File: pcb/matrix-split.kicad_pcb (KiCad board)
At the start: 2 copper layers, 160.1 x 127.5 mm, 115 parts, among them J1 AudioJack4, J4 DBG, SW1 Switch, SW10 Switch, SW11 Switch, SW12 Switch, SW13 Switch, SW14 Switch, SW15 Switch, SW16 Switch, SW17 Switch, SW18 Switch, SW19 Switch, SW2 Switch, SW20 Switch, SW21 Switch, SW22 Switch, SW23 Switch, SW24 Switch, SW25 Switch, SW26 Switch, SW27 Switch, SW28 Switch, SW29 Switch, SW3 Switch, SW30 Reset_Switch, SW31 BootSel_Switch, SW4 Switch, SW5 Switch, SW6 Switch, SW7 Switch, SW8 Switch, SW9 Switch, U1 W25Q128JVS, U2 RP2040, U3 NCP1117-3.3_SOT223, Y1 Crystal_GND24

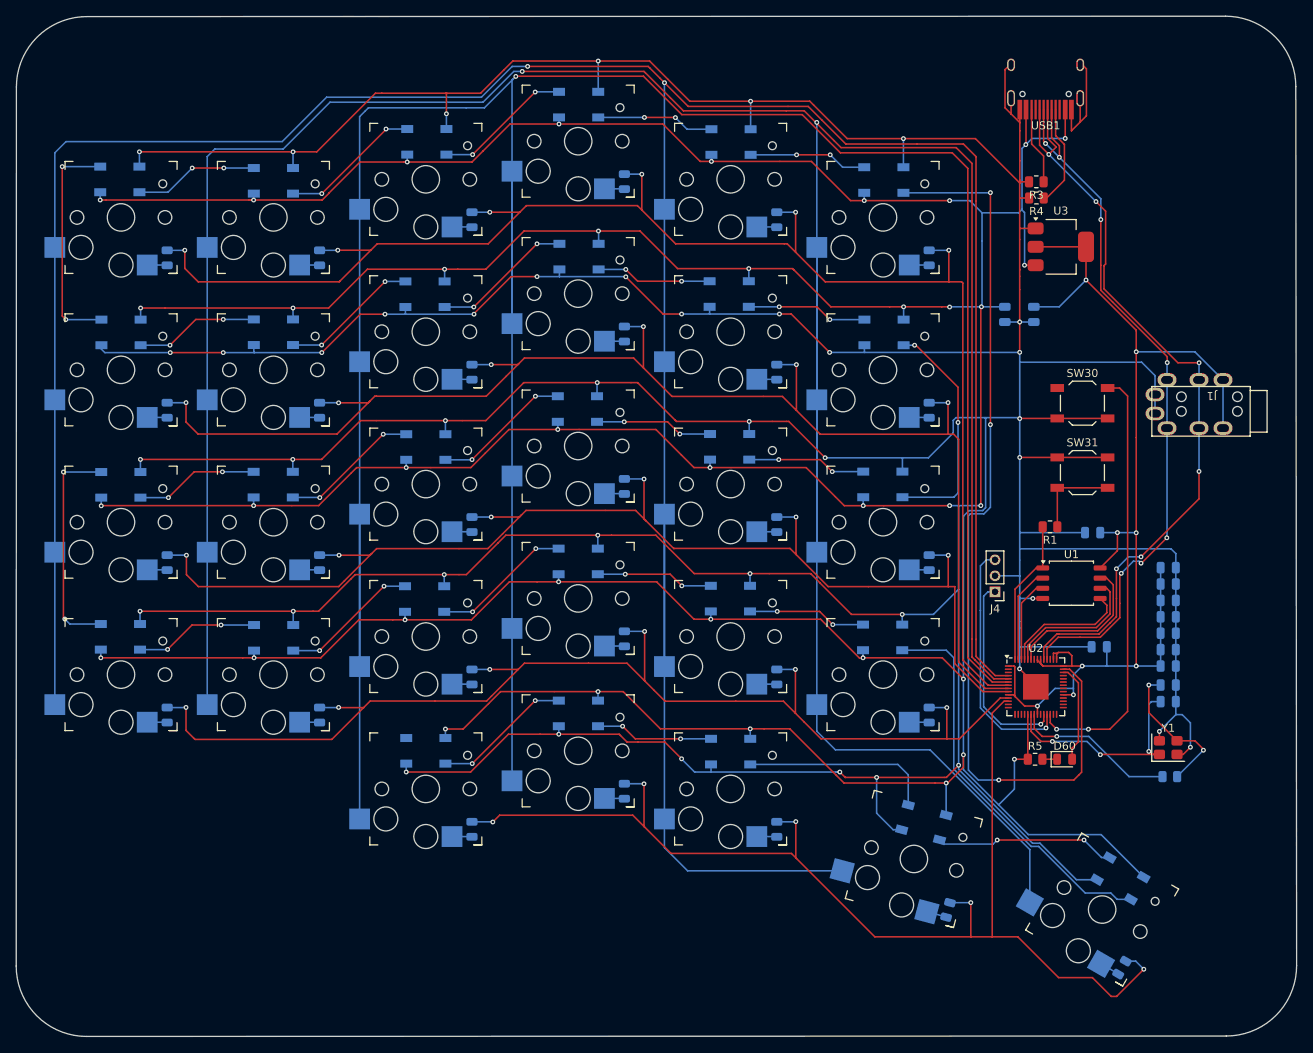
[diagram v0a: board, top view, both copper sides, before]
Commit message: updating routing and pcb layout
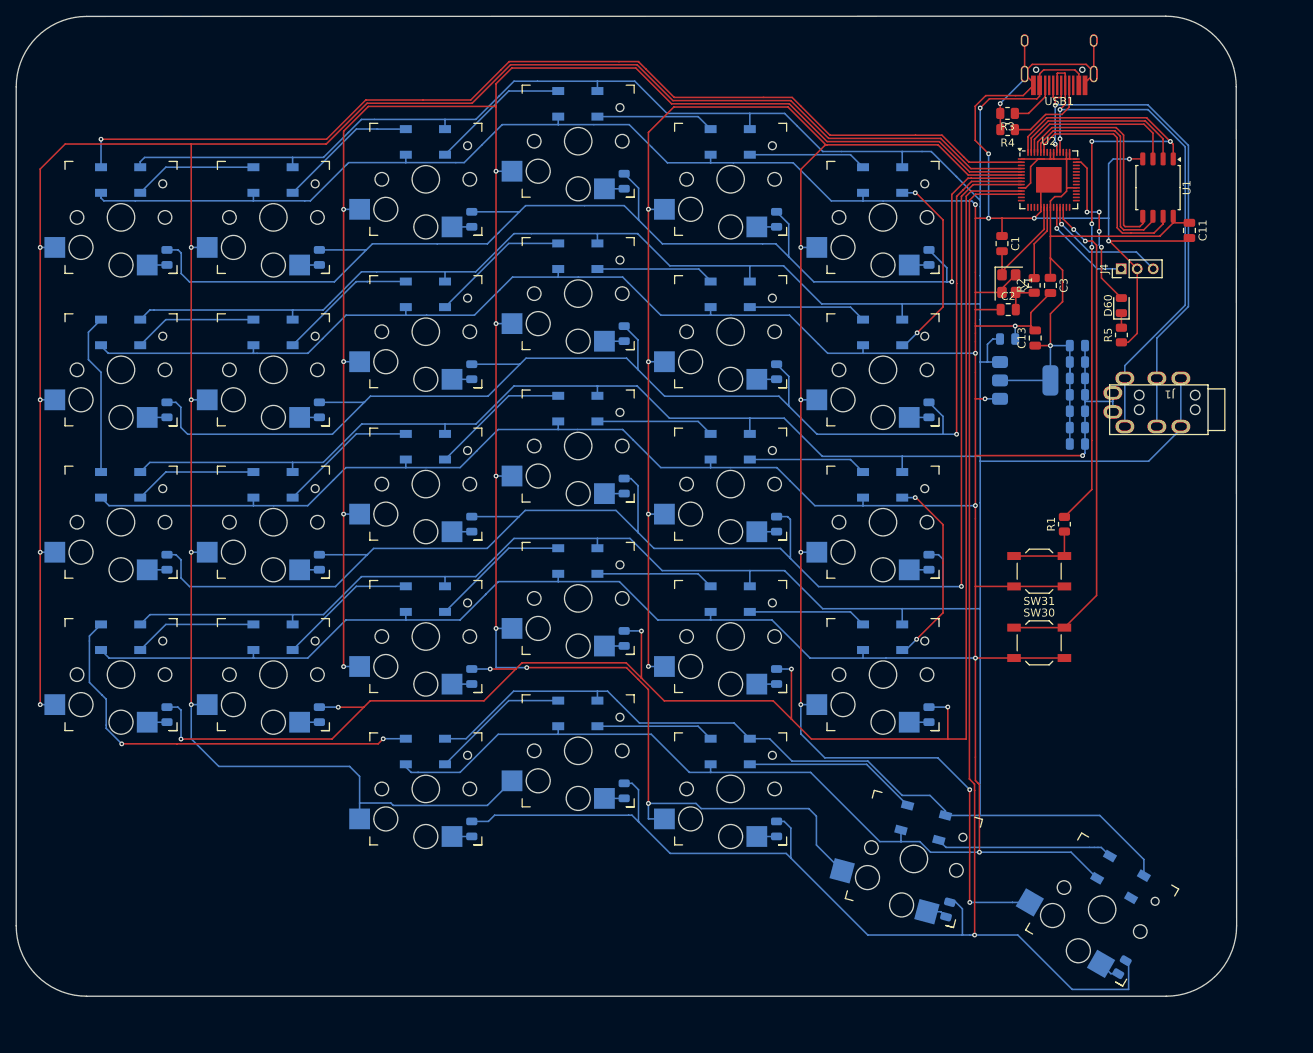
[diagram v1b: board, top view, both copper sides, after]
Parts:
- removed D31, D32, D33, D34, D35, D36, D37, D38, D39, D40, D41, D42, D43, D44, D45, D46, D47, D48, D49, D50, D51, D52, D53, D54, D55, D56, D57, D58, D59: SK6812, LED_SMD:LED_SK6812_PLCC4_5.0x5.0mm_P3.2mm
- added SKD1: SK6812, LED_SMD:LED_SK6812_PLCC4_5.0x5.0mm_P3.2mm, B.Cu at (38.0, 43.0)
- added SKD10: SK6812, LED_SMD:LED_SK6812_PLCC4_5.0x5.0mm_P3.2mm, B.Cu at (95.2, 52.5)
- added SKD11: SK6812, LED_SMD:LED_SK6812_PLCC4_5.0x5.0mm_P3.2mm, B.Cu at (114.2, 57.2)
- added SKD12: SK6812, LED_SMD:LED_SK6812_PLCC4_5.0x5.0mm_P3.2mm, B.Cu at (133.3, 62.0)
- added SKD13: SK6812, LED_SMD:LED_SK6812_PLCC4_5.0x5.0mm_P3.2mm, B.Cu at (38.0, 81.0)
- added SKD14: SK6812, LED_SMD:LED_SK6812_PLCC4_5.0x5.0mm_P3.2mm, B.Cu at (57.1, 81.0)
- added SKD15: SK6812, LED_SMD:LED_SK6812_PLCC4_5.0x5.0mm_P3.2mm, B.Cu at (76.2, 76.3)
- added SKD16: SK6812, LED_SMD:LED_SK6812_PLCC4_5.0x5.0mm_P3.2mm, B.Cu at (95.2, 71.5)
- added SKD17: SK6812, LED_SMD:LED_SK6812_PLCC4_5.0x5.0mm_P3.2mm, B.Cu at (114.2, 76.3)
- added SKD18: SK6812, LED_SMD:LED_SK6812_PLCC4_5.0x5.0mm_P3.2mm, B.Cu at (133.3, 81.0)
- added SKD19: SK6812, LED_SMD:LED_SK6812_PLCC4_5.0x5.0mm_P3.2mm, B.Cu at (38.0, 100.1)
- added SKD2: SK6812, LED_SMD:LED_SK6812_PLCC4_5.0x5.0mm_P3.2mm, B.Cu at (57.1, 43.0)
- added SKD20: SK6812, LED_SMD:LED_SK6812_PLCC4_5.0x5.0mm_P3.2mm, B.Cu at (57.1, 100.1)
- added SKD21: SK6812, LED_SMD:LED_SK6812_PLCC4_5.0x5.0mm_P3.2mm, B.Cu at (76.2, 95.3)
- added SKD22: SK6812, LED_SMD:LED_SK6812_PLCC4_5.0x5.0mm_P3.2mm, B.Cu at (95.2, 90.6)
- added SKD23: SK6812, LED_SMD:LED_SK6812_PLCC4_5.0x5.0mm_P3.2mm, B.Cu at (114.2, 95.3)
- added SKD24: SK6812, LED_SMD:LED_SK6812_PLCC4_5.0x5.0mm_P3.2mm, B.Cu at (133.3, 100.1)
- added SKD25: SK6812, LED_SMD:LED_SK6812_PLCC4_5.0x5.0mm_P3.2mm, B.Cu at (76.2, 114.4)
- added SKD26: SK6812, LED_SMD:LED_SK6812_PLCC4_5.0x5.0mm_P3.2mm, B.Cu at (95.2, 109.6)
- added SKD27: SK6812, LED_SMD:LED_SK6812_PLCC4_5.0x5.0mm_P3.2mm, B.Cu at (114.2, 114.4)
- added SKD28: SK6812, LED_SMD:LED_SK6812_PLCC4_5.0x5.0mm_P3.2mm, B.Cu at (138.4, 123.3)
- added SKD29: SK6812, LED_SMD:LED_SK6812_PLCC4_5.0x5.0mm_P3.2mm, B.Cu at (163.0, 130.1)
- added SKD3: SK6812, LED_SMD:LED_SK6812_PLCC4_5.0x5.0mm_P3.2mm, B.Cu at (76.2, 38.2)
- added SKD4: SK6812, LED_SMD:LED_SK6812_PLCC4_5.0x5.0mm_P3.2mm, B.Cu at (95.2, 33.4)
- added SKD5: SK6812, LED_SMD:LED_SK6812_PLCC4_5.0x5.0mm_P3.2mm, B.Cu at (114.2, 38.2)
- added SKD6: SK6812, LED_SMD:LED_SK6812_PLCC4_5.0x5.0mm_P3.2mm, B.Cu at (133.3, 43.0)
- added SKD7: SK6812, LED_SMD:LED_SK6812_PLCC4_5.0x5.0mm_P3.2mm, B.Cu at (38.0, 62.0)
- added SKD8: SK6812, LED_SMD:LED_SK6812_PLCC4_5.0x5.0mm_P3.2mm, B.Cu at (57.1, 62.0)
- added SKD9: SK6812, LED_SMD:LED_SK6812_PLCC4_5.0x5.0mm_P3.2mm, B.Cu at (76.2, 57.2)
- C1, C11, C13, C2, C3, R2: moved to F.Cu
- SW1, SW10, SW11, SW12, SW13, SW14, SW15, SW16, SW17, SW18, SW19, SW2, SW20, SW21, SW22, SW23, SW24, SW25, SW26, SW27, SW28, SW29, SW3, SW4, SW5, SW6, SW7, SW8, SW9: footprint keyswitches.pretty-master:Kailh_socket_PG1350 -> keyswitches:Kailh_socket_PG1350
- U3: moved to B.Cu
- USB1: footprint Type-C.pretty-master:HRO-TYPE-C-31-M-12-HandSoldering -> Type-C:HRO-TYPE-C-31-M-12-HandSoldering
- moved R2 63.7 mm to (152.2, 56.1), turned to 90 degrees
- moved U2 63.4 mm to (154.1, 42.9)
- moved Y1 61.3 mm to (149.1, 55.9), turned to -90 degrees
- moved C1 60.9 mm to (148.2, 50.9), turned to -90 degrees
- moved D1 58.0 mm to (43.8, 52.6)
- moved D13 58.0 mm to (43.8, 90.7)
- moved D19 58.0 mm to (43.8, 109.8)
- moved D7 58.0 mm to (43.8, 71.7)
- moved SW19 57.9 mm to (38.1, 104.8)
- moved SW22 57.9 mm to (95.2, 95.2)
- moved SW1 57.9 mm to (38.1, 47.6)
- moved SW10 57.9 mm to (95.2, 57.1)
- moved SW13 57.9 mm to (38.1, 85.7)
- moved SW16 57.9 mm to (95.2, 76.2)
- moved SW4 57.9 mm to (95.2, 38.1)
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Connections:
- J1 pad S: VCC -> VBUS
- U2 pad 2: unconnected-(U2-GPIO0-Pad2) -> LED
- U2 pad 4: COL2 -> COL1
- U2 pad 40: STATUS_LED -> unconnected-(U2-GPIO28_ADC2-Pad40)
- U2 pad 41: LED -> STATUS_LED
- U2 pad 5: COL3 -> COL2
- U2 pad 6: COL1 -> COL3
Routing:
- net COL3: track 413.2 -> 254.9 mm, vias 2 -> 10
- net COL2: track 398.9 -> 316.3 mm, vias 2 -> 10
- net ROW4: track 152.4 -> 220.2 mm
- net Q_SS: track 18.5 -> 82.5 mm, vias 0 -> 4
- net VCC: track 154.9 -> 93.6 mm, vias 8 -> 1
- net ROW5: track 150.2 -> 211.3 mm, vias 5 -> 1
- net Net-(SKD19-DIN): track 0.00 -> 53.0 mm, vias 0 -> 2
- net Net-(D54-DOUT): track 49.6 -> 0.00 mm
- net GND: track 916.3 -> 872.4 mm, vias 43 -> 14
- net ROW1: track 197.5 -> 159.1 mm, vias 6 -> 1
- net ROW3: track 161.2 -> 199.1 mm, vias 6 -> 1
- net TX: track 97.2 -> 66.5 mm, vias 6 -> 2
- net Net-(D42-DOUT): track 29.4 -> 0.00 mm, vias 2 -> 0
- net Net-(D36-DOUT): track 28.5 -> 0.00 mm, vias 2 -> 0
- net Net-(D48-DOUT): track 27.9 -> 0.00 mm, vias 2 -> 0
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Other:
- board size 160.1 x 127.5 mm -> 152.6 x 122.5 mm

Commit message: making kb reversible
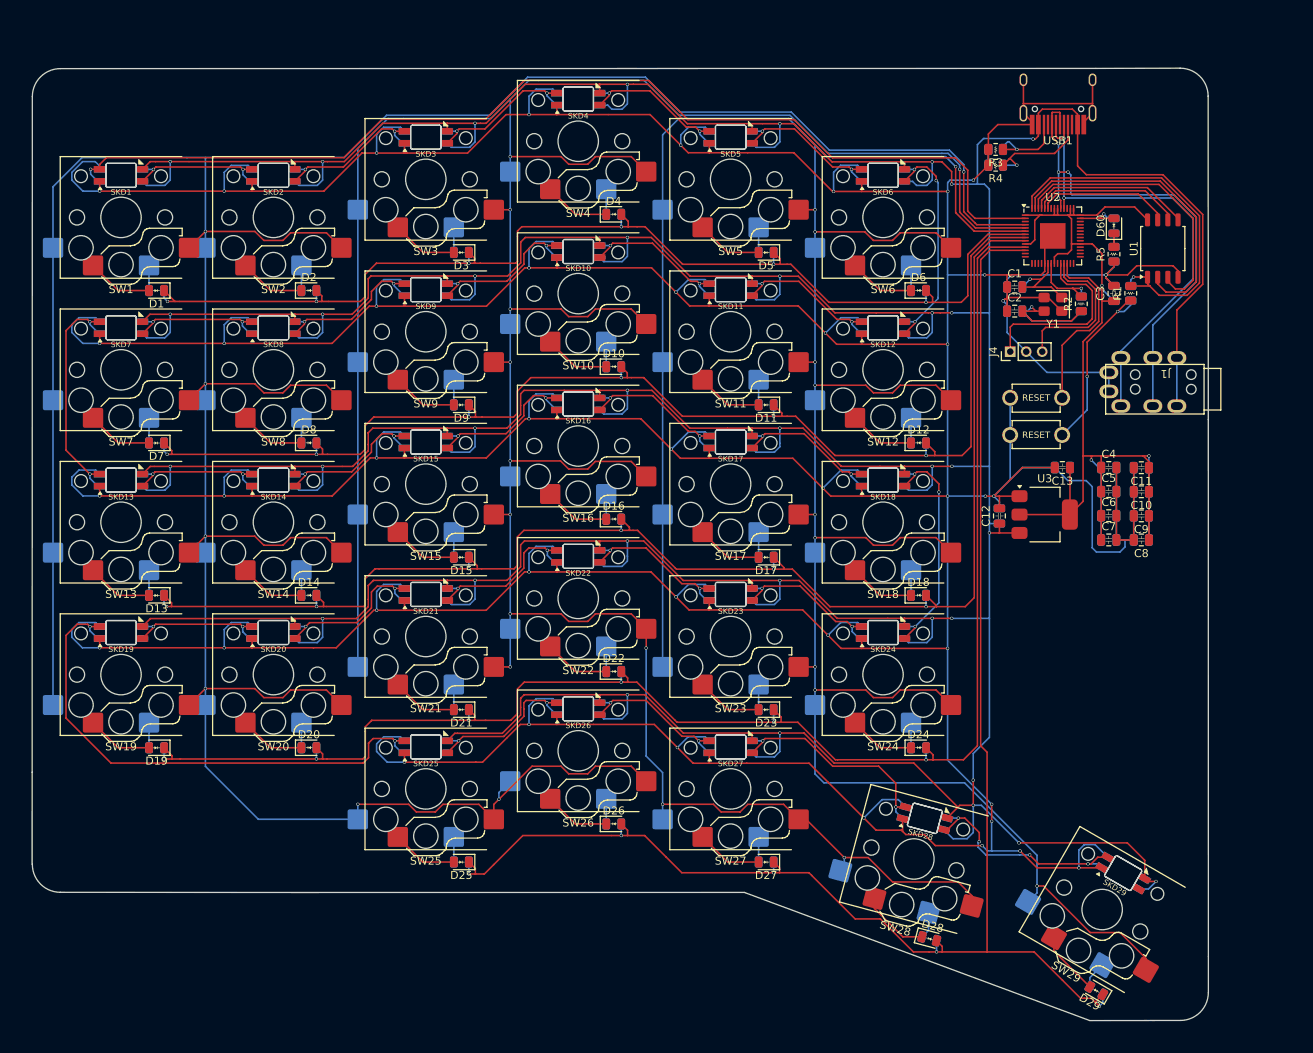
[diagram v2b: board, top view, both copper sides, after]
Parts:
- C1, C11, C13, C2, C3: footprint Capacitor_SMD:C_0805_2012Metric -> custom_parts:C_0805_2012Metric-Reversible
- C10, C12, C4, C5, C6, C7, C8, C9: footprint Capacitor_SMD:C_0805_2012Metric -> custom_parts:C_0805_2012Metric-Reversible; moved to F.Cu
- D1, D10, D11, D12, D13, D14, D15, D16, D17, D18, D19, D2, D20, D21, D22, D23, D24, D25, D26, D27, D28, D29, D3, D4, D5, D6, D7, D8, D9: footprint Diode_SMD:D_0805_2012Metric -> custom_parts:D_0805_2012Metric-Reversible; moved to F.Cu
- D60: footprint LED_SMD:LED_0805_2012Metric -> custom_parts:D_0805_2012Metric-Reversible
- R1, R2, R3, R4, R5: footprint Resistor_SMD:R_0805_2012Metric -> custom_parts:R_0805_2012Metric-Reversible
- SKD1, SKD10, SKD11, SKD12, SKD13, SKD14, SKD15, SKD16, SKD17, SKD18, SKD19, SKD2, SKD20, SKD21, SKD22, SKD23, SKD24, SKD25, SKD26, SKD27, SKD28, SKD29, SKD3, SKD4, SKD5, SKD6, SKD7, SKD8, SKD9: footprint LED_SMD:LED_SK6812_PLCC4_5.0x5.0mm_P3.2mm -> custom_parts:SK6812-MINI-E-Reversible; moved to F.Cu
- SW1, SW10, SW11, SW12, SW13, SW14, SW15, SW16, SW17, SW18, SW19, SW2, SW20, SW21, SW22, SW23, SW24, SW25, SW26, SW27, SW28, SW29, SW3, SW4, SW5, SW6, SW7, SW8, SW9: footprint keyswitches:Kailh_socket_PG1350 -> custom_parts:SW_Hotswap_Kailh_Choc_V1V2-Reversible
- SW30, SW31: footprint Button_Switch_SMD:SW_SPST_TL3342 -> SofleKeyboard-footprint:TACT_SWITCH_TVBP06
- U3: moved to F.Cu
- Y1: value Crystal_GND24 -> ABM8-272-T3
- moved SW30 30.6 mm to (152.5, 70.2), turned to 180 degrees
- moved C11 30.3 mm to (165.6, 78.9), turned to 180 degrees
- moved R1 30.0 mm to (164.3, 57.1)
- moved C12 22.1 mm to (147.9, 84.9), turned to 90 degrees
- moved C8 21.7 mm to (165.6, 87.9), turned to 180 degrees
- moved C9 20.8 mm to (165.6, 84.9), turned to 180 degrees
- moved C10 19.9 mm to (165.6, 81.9), turned to 180 degrees
- moved C7 18.6 mm to (161.6, 87.9)
- moved J4 17.3 mm to (149.2, 64.4)
- moved SW31 17.0 mm to (152.5, 74.8), turned to 0 degrees
- moved U3 16.9 mm to (153.6, 84.8)
- moved C13 16.5 mm to (155.8, 78.9), turned to 180 degrees
- moved C6 13.6 mm to (161.6, 84.9)
- moved R5 10.1 mm to (162.2, 52.2)
- moved D60 10.0 mm to (162.2, 48.7)
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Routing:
- net GND: track 872.4 -> 1087.9 mm, vias 14 -> 43
- net VBUS: track 733.3 -> 917.2 mm, vias 1 -> 35
- net COL1: track 338.8 -> 434.9 mm, vias 8 -> 7
- net COL3: track 254.9 -> 340.1 mm
- net COL2: track 316.3 -> 388.3 mm, vias 10 -> 12
- net VCC: track 93.6 -> 138.6 mm, vias 1 -> 3
- net SW_RST: track 62.8 -> 22.7 mm, vias 2 -> 0
- net Q_SS: track 82.5 -> 47.7 mm, vias 4 -> 1
- net ROW4: track 220.2 -> 201.1 mm
- net Net-(C2-Pad2): track 4.50 -> 21.6 mm, vias 0 -> 1
- net Q_SD1: track 22.6 -> 38.9 mm
- net ROW3: track 199.1 -> 183.1 mm, vias 1 -> 6
- net Q_SD2: track 20.9 -> 35.3 mm
- net ROW1: track 159.1 -> 145.0 mm, vias 1 -> 6
- net STATUS_LED: track 20.5 -> 6.65 mm, vias 4 -> 1
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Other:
- board size 152.6 x 122.5 mm -> 147 x 119.1 mm

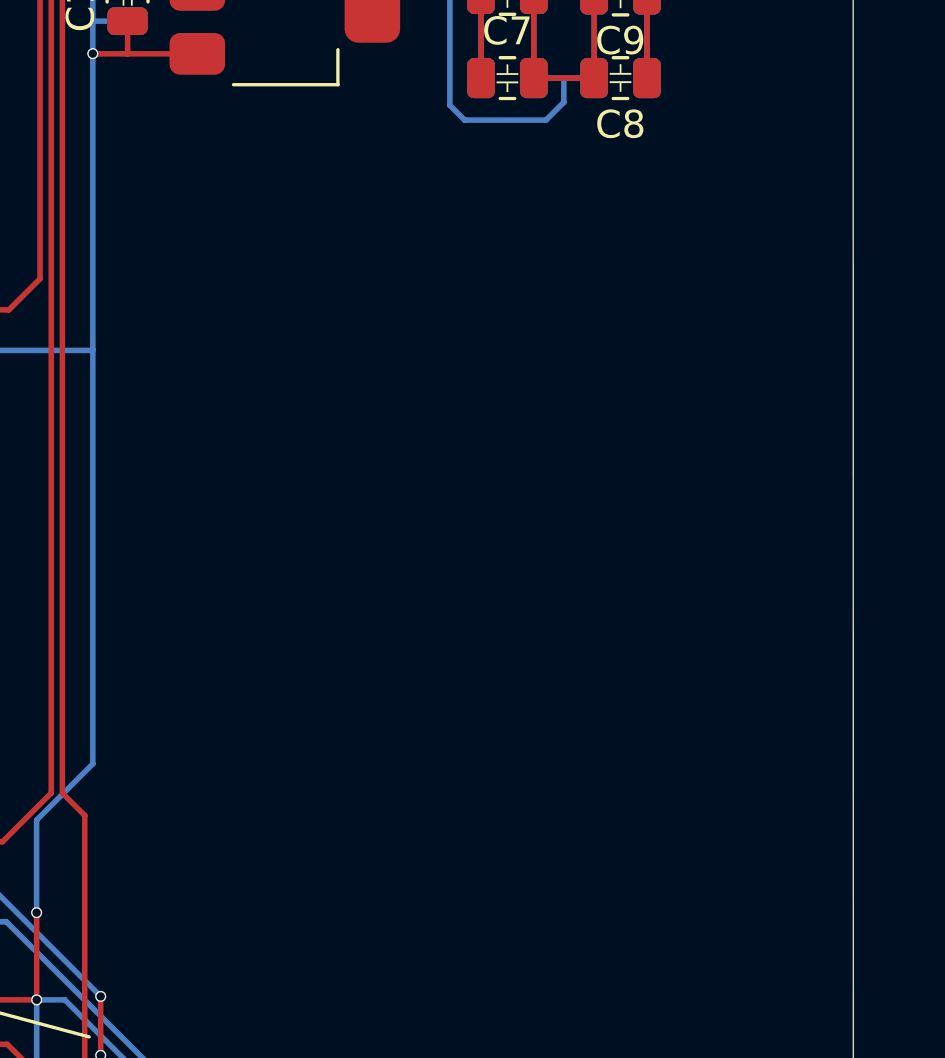
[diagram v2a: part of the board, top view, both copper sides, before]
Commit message: adding qr code and finalizing rev1
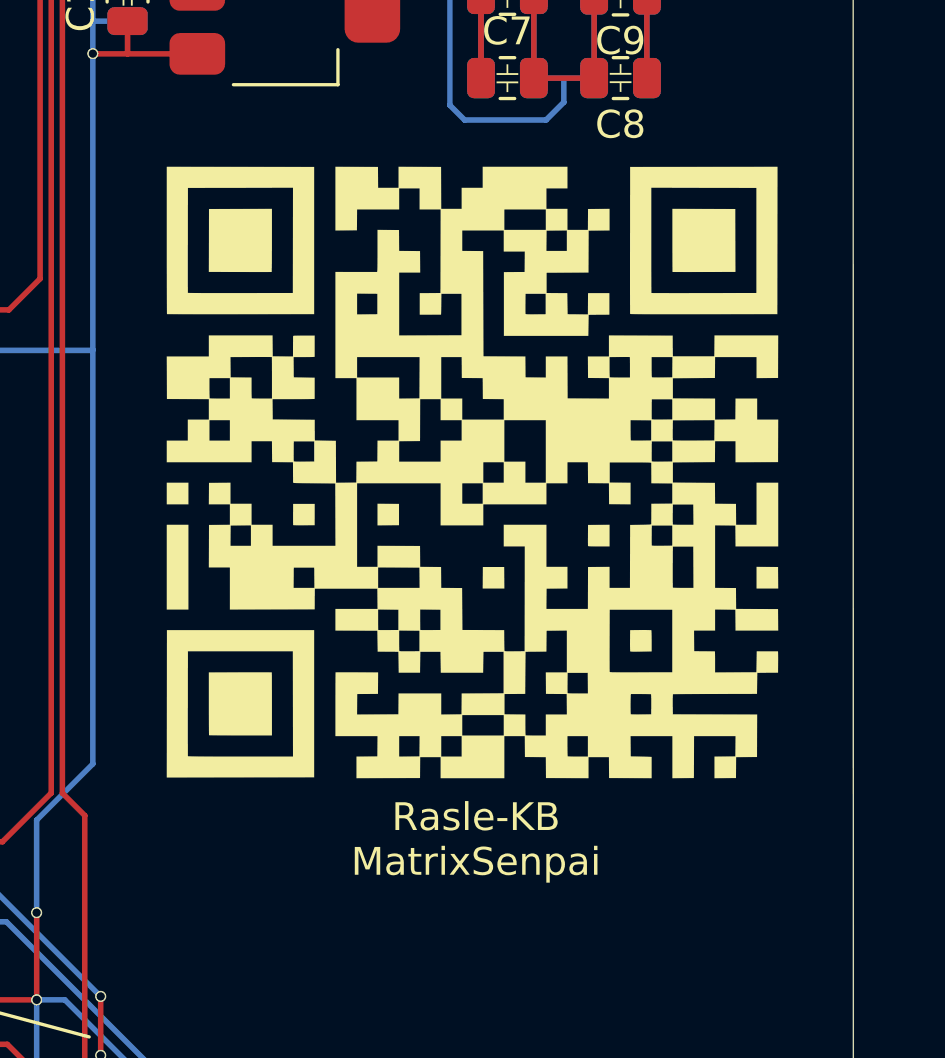
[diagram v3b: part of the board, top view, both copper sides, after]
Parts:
- added G***: LOGO, custom_parts:qrcode, F.Cu at (160.3, 102.1)
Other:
- board text added: "Rasle-KB MatrixSenpai"
